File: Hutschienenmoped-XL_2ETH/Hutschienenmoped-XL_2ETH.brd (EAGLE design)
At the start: 166.3 x 101.8 mm, 129 parts, among them J1 638207222005, J13 638207222005, J15 638207222008, J2 645004114822, J4 61300421121, J7 638207222005, J8 638207222007, U4 TLE9250VSJ

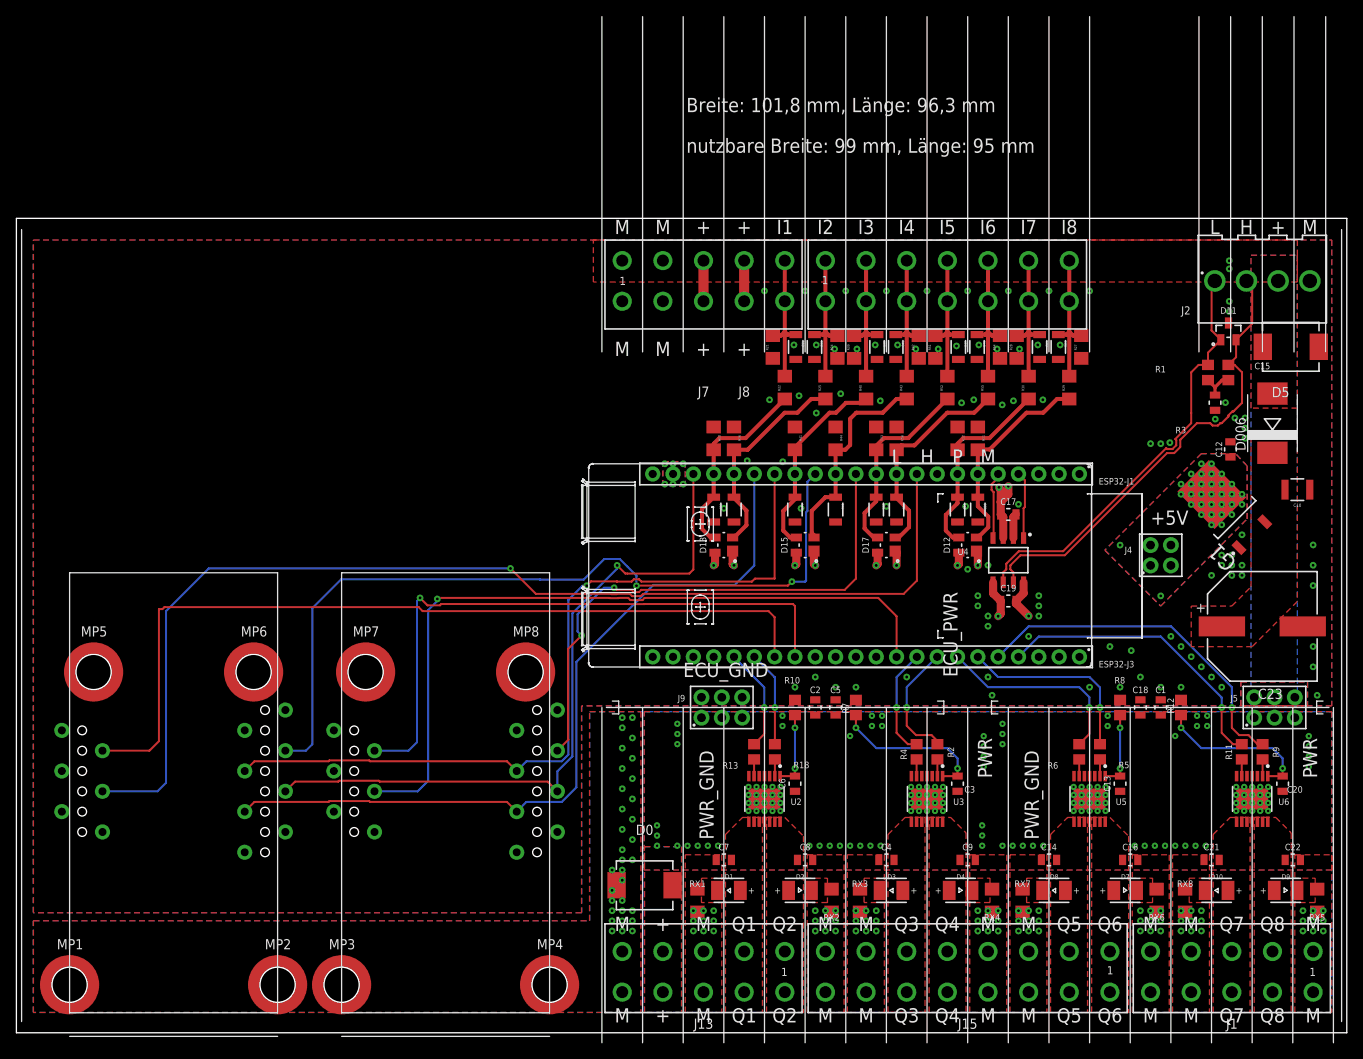
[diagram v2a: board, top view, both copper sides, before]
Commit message: Change grid settings to 50mm, hide grid display. Simplify wire connections in the layout for better clarity and organization. Adjust polygon widths for consistency and isolate values. Add vias for improved routing efficiency.
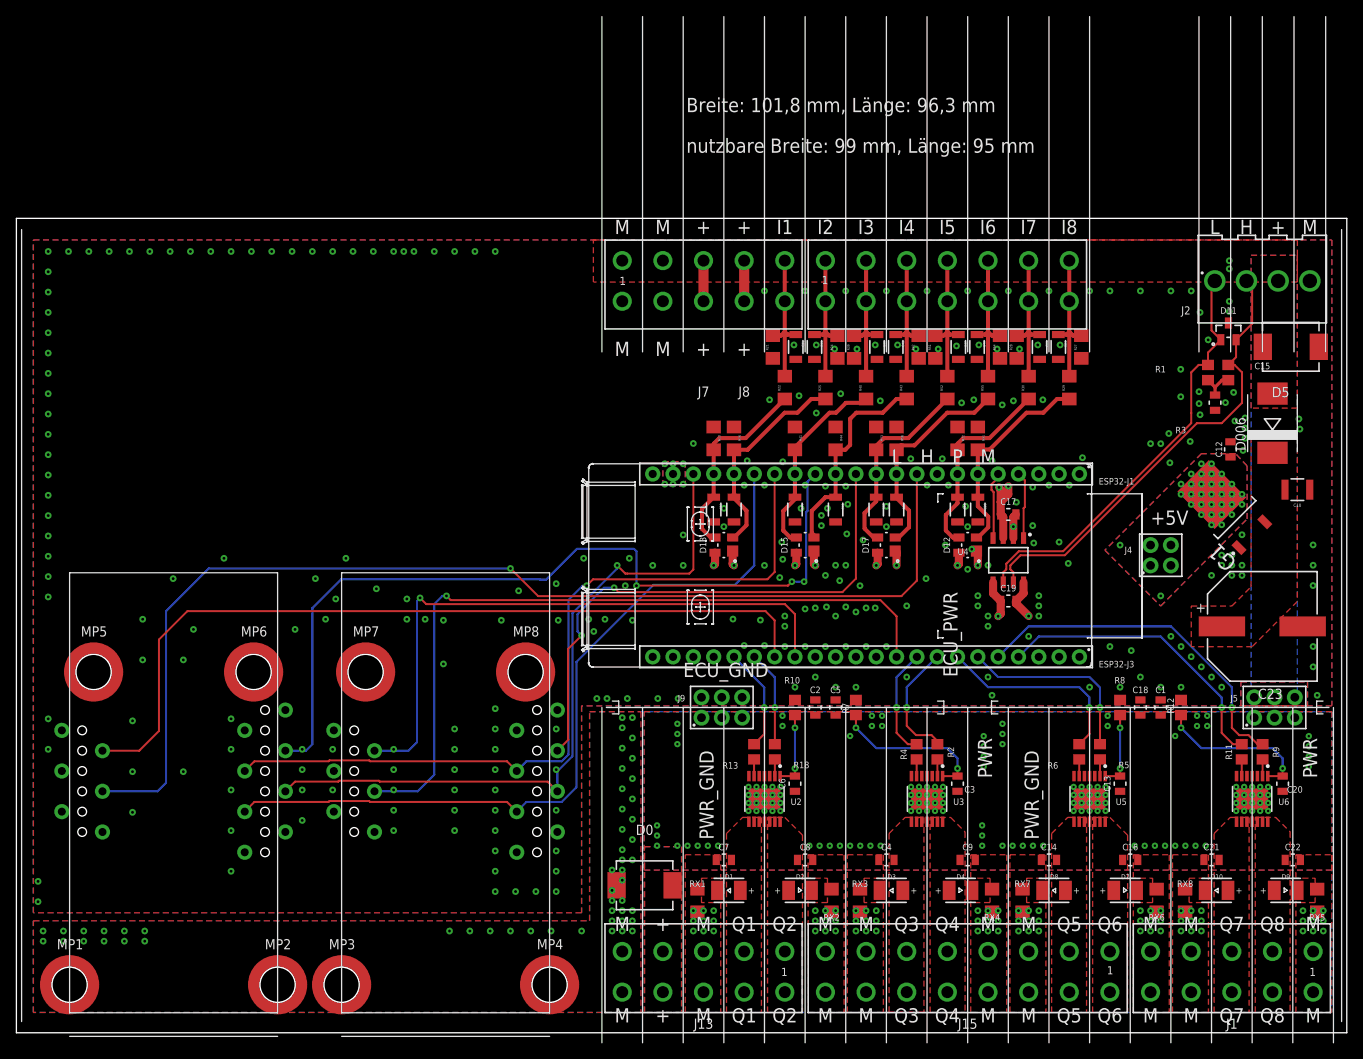
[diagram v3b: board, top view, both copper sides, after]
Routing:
- net INT0: track 106.6 -> 103.0 mm
- net CS0: track 101.2 -> 104.1 mm
- net CAN_P: track 58.4 -> 57.6 mm
- net INT1: track 77.7 -> 77.0 mm
- net SCLK: track 102.0 -> 101.2 mm
- net CAN_N: track 54.2 -> 53.5 mm
- net ECU_GND: vias 104 -> 308

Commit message: Update grid settings and layer visibility. Adjust attributes of elements C15, D5, R1, R3.
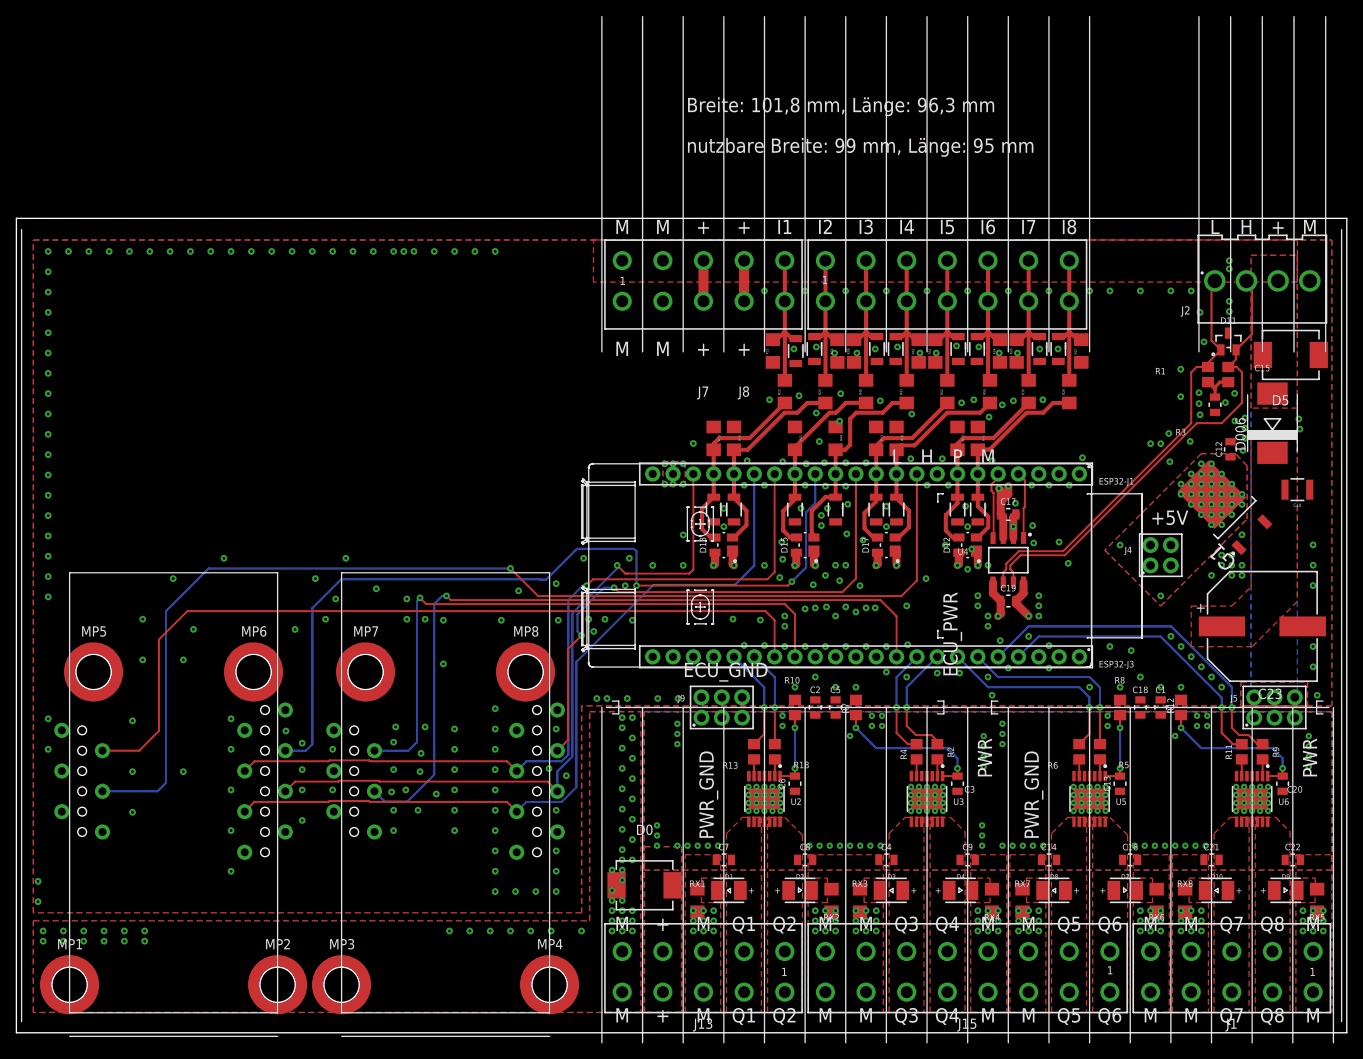
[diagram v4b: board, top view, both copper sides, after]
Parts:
- moved D11 1.27 mm to (80.9, 86.4)
- moved D5 1.02 mm to (88.6, 84.7)
- moved R55 0.57 mm to (51.1, 80.1)
- moved C31 0.51 mm to (26.8, 85.2)
- moved R21 0.51 mm to (23.9, 85.2)
- moved R22 0.51 mm to (25.4, 80.1)
- moved R24 0.51 mm to (32.0, 85.2)
- moved R25 0.51 mm to (30.5, 80.1)
- moved R27 0.51 mm to (62.5, 85.2)
- moved R28 0.51 mm to (54.4, 85.2)
- moved R29 0.51 mm to (61.0, 80.1)
- moved R30 0.51 mm to (55.9, 80.1)
- moved R39 0.51 mm to (34.1, 85.2)
- moved R40 0.51 mm to (35.6, 80.1)
- moved R42 0.51 mm to (42.1, 85.2)
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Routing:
- net RST1: track 94.0 -> 95.1 mm
- net CS0: track 104.1 -> 103.1 mm
- net I6: track 17.7 -> 18.6 mm
- net I1: track 17.7 -> 18.6 mm
- net I2: track 17.7 -> 18.5 mm
- net I7: track 17.7 -> 18.5 mm
- net I4: track 17.7 -> 18.5 mm
- net I3: track 17.7 -> 18.5 mm
- net I8: track 17.7 -> 18.5 mm
- net I5: track 17.7 -> 18.5 mm
- net +5V: track 82.3 -> 83.0 mm
- net ECU_GND: vias 308 -> 333
